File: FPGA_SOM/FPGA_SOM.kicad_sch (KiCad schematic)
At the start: 58 parts, among them J1 Conn_01x12, J2 Conn_02x05_Counter_Clockwise, J3 Conn_01x06, J5 Conn_01x02, J7 Conn_01x09, J8 Conn_01x10, U1 ICE40UP5K-SG48ITR, U101 W25X20CLSN, U2 AP2127N-3.3, U3 AP2127N-1.2, X101 ECS-2520MV-xxx-xx

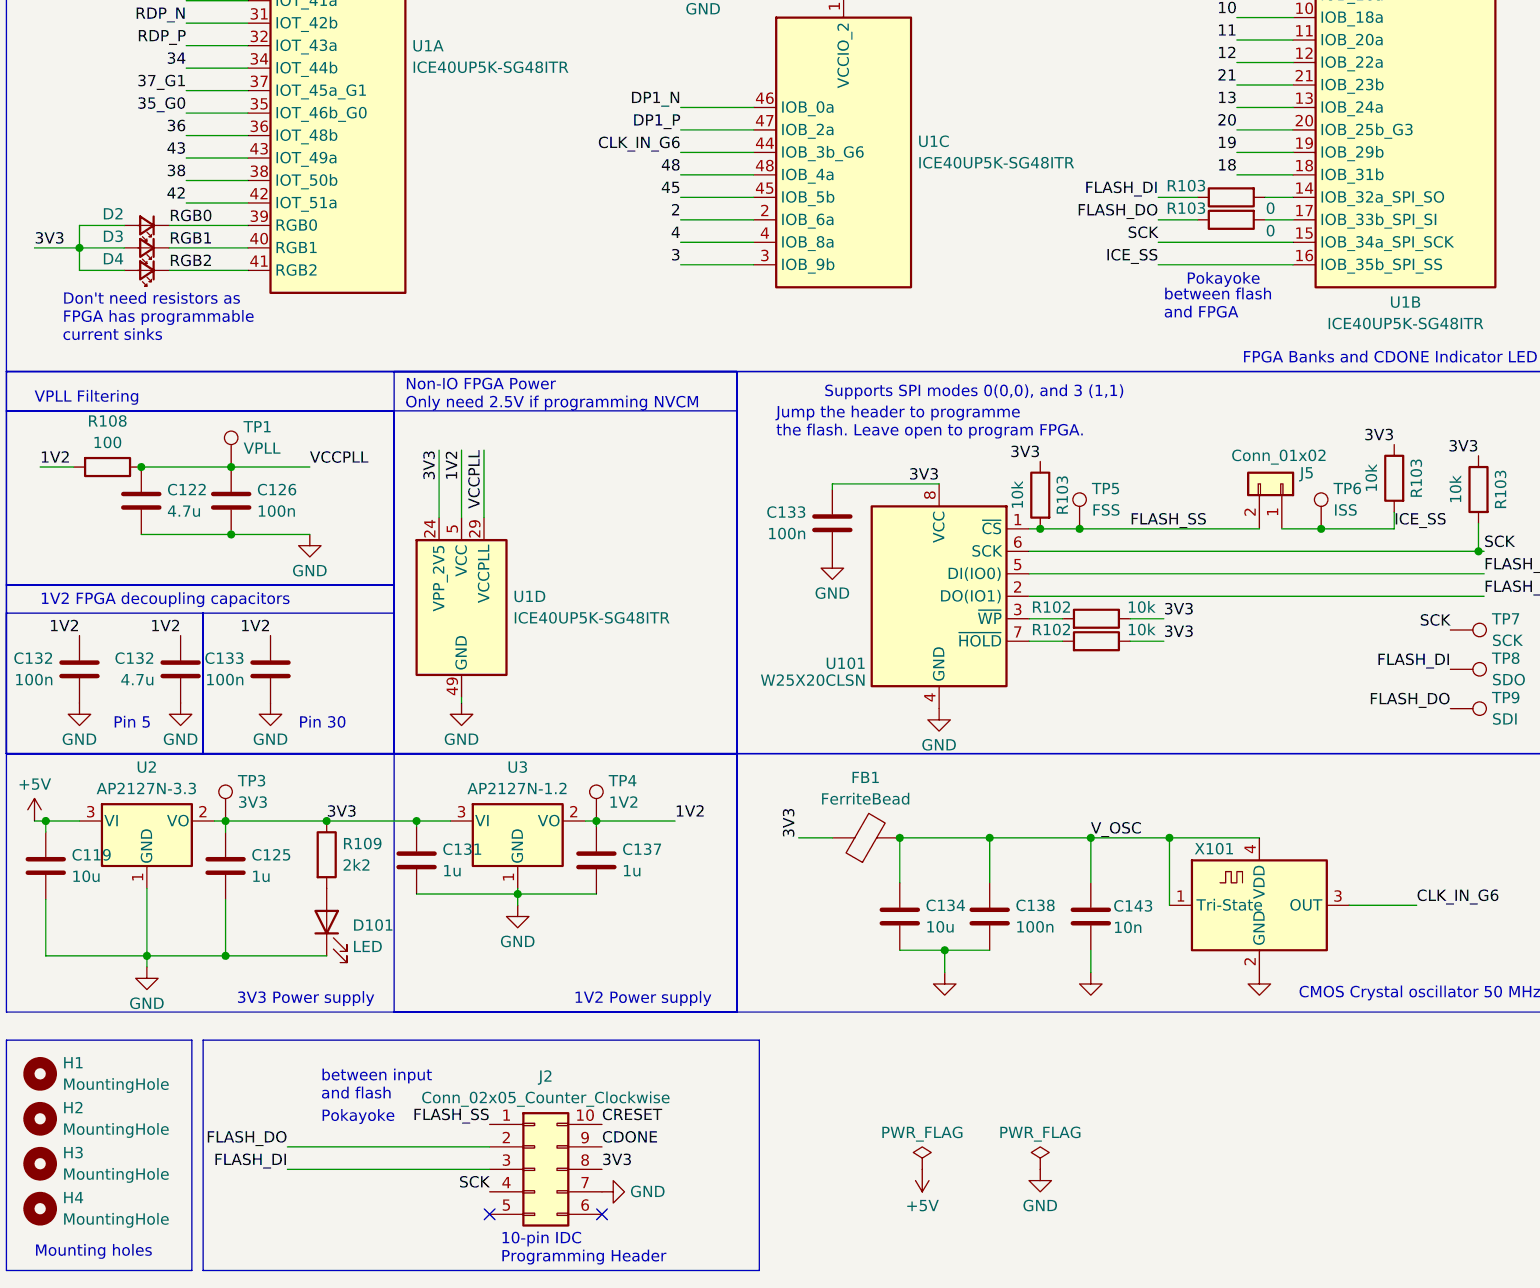
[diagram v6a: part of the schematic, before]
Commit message: Added button and clarified silkscreen for RGB leds.
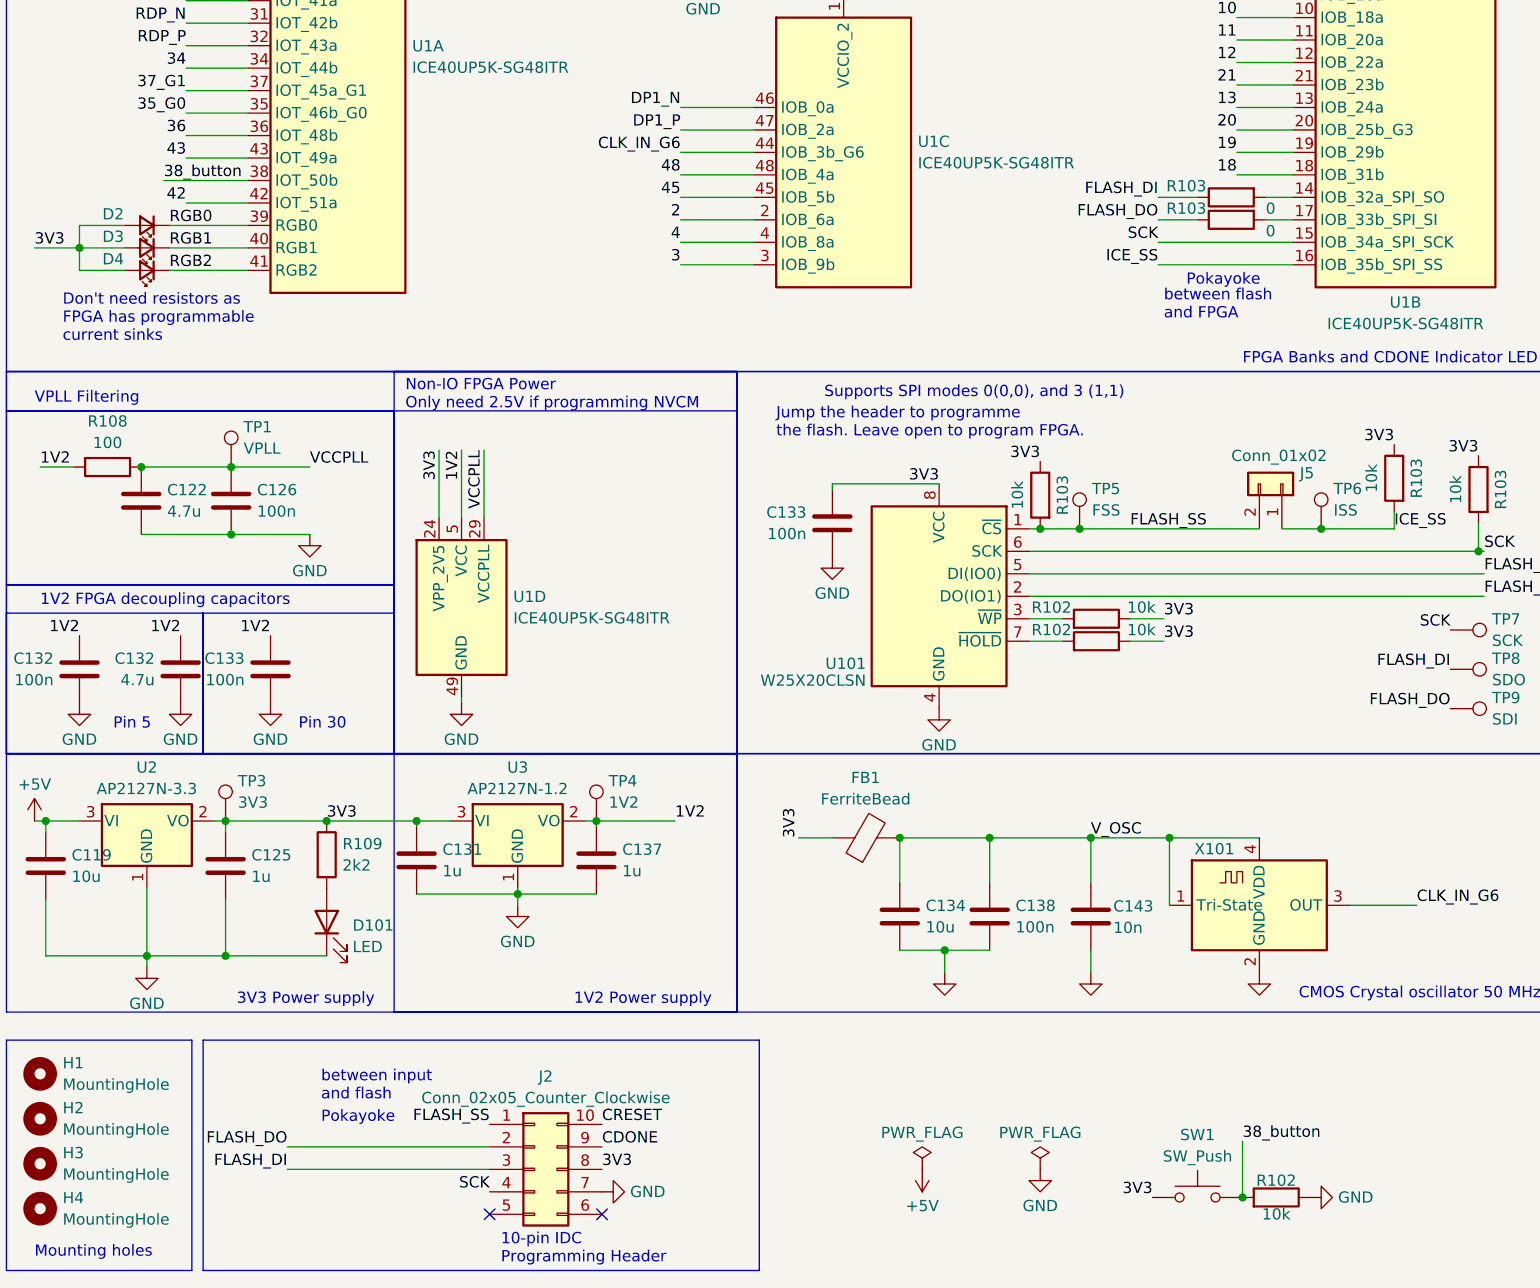
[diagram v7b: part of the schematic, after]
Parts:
- added R102: 10k, Resistor_SMD:R_0603_1608Metric, symbol Device:R
- added SW1: SW_Push, Button_Switch_THT:SW_PUSH_6mm, symbol Switch:SW_Push
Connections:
- net 38: no longer U1.38 (IOT_50b)
- net 3V3: now also SW1.1
- net GND: now also R102.1
- new net 38_button: R102.2, SW1.2, U1.38 (IOT_50b)
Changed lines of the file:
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@@
   (junction (at 155.575 19.685) (diameter 0) (color 0 0 0 0)
+  )
+  (junction (at 153.035 186.69) (diameter 0) (color 0 0 0 0)
   )
   (junction (at 49.53 144.145) (diameter 0) (color 0 0 0 0)
@@
     (stroke (width 0) (type default))
   )
+  (wire (pts (xy 153.035 180.34) (xy 153.035 186.69))
+    (stroke (width 0) (type default))
+  )
   (wire (pts (xy 143.51 78.74) (xy 158.75 78.74))
     (stroke (width 0) (type default))
@@
     (stroke (width 0) (type default))
   )
-  (wire (pts (xy 33.655 71.755) (xy 40.64 71.755))
+  (wire (pts (xy 31.115 71.755) (xy 40.64 71.755))
     (stroke (width 0) (type default))
   )
@@
     (effects (font (size 1.27 1.27)) (justify left bottom))
   )
-  (label "38" (at 33.655 71.755 180) (fields_autoplaced)
-    (effects (font (size 1.27 1.27)) (justify right bottom))
-  )
   (label "20" (at 152.4 66.04 180) (fields_autoplaced)
     (effects (font (size 1.27 1.27)) (justify right bottom))
@@
     (effects (font (size 1.27 1.27)) (justify left bottom))
   )
+  (label "3V3" (at 142.875 186.69 180) (fields_autoplaced)
+    (effects (font (size 1.27 1.27)) (justify right bottom))
+  )
   (label "FLASH_DI" (at 143.51 73.66 180) (fields_autoplaced)
     (effects (font (size 1.27 1.27)) (justify right bottom))
@@
     (effects (font (size 1.27 1.27)) (justify right bottom))
   )
+  (label "38_button" (at 31.115 71.755 0) (fields_autoplaced)
+    (effects (font (size 1.27 1.27)) (justify left bottom))
+  )
   (label "CDONE" (at 80.645 180.975 0) (fields_autoplaced)
     (effects (font (size 1.27 1.27)) (justify left bottom))
@@
   )
   (label "RGB0" (at 31.75 76.835 0) (fields_autoplaced)
+    (effects (font (size 1.27 1.27)) (justify left bottom))
+  )
+  (label "38_button" (at 153.035 180.34 0) (fields_autoplaced)
     (effects (font (size 1.27 1.27)) (justify left bottom))
   )
@@
     )
   )
+  (symbol (lib_id "Switch:SW_Push") (at 147.955 186.69 0) (unit 1)
+    (in_bom yes) (on_board yes) (dnp no) (fields_autoplaced)
+    (property "Reference" "SW1" (at 147.955 179.6247 0)
+      (effects (font (size 1.27 1.27)))
+    )
+    (property "Value" "SW_Push" (at 147.955 182.0489 0)
+      (effects (font (size 1.27 1.27)))
+    )
+    (property "Footprint" "Button_Switch_THT:SW_PUSH_6mm" (at 147.955 181.61 0)
+      (effects (font (size 1.27 1.27)) hide)
+    )
+    (property "Datasheet" "~" (at 147.955 181.61 0)
+      (effects (font (size 1.27 1.27)) hide)
+    )
+    (pin "1")
+    (pin "2")
+    (instances
+      (project "FPGA_SOM"
+        (path "/c9513ae4-ec90-4b73-ae24-d135d02c4e68"
+          (reference "SW1") (unit 1)
+        )
+      )
+    )
+  )
   (symbol (lib_id "Device:C") (at 28.575 107.95 0) (unit 1)
     (in_bom yes) (on_board yes) (dnp no)
@@
         (path "/c9513ae4-ec90-4b73-ae24-d135d02c4e68"
           (reference "#PWR06") (unit 1)
+        )
+      )
+    )
+  )
+  (symbol (lib_id "power:GND") (at 160.655 186.69 90) (unit 1)
+    (in_bom yes) (on_board yes) (dnp no) (fields_autoplaced)
+    (property "Reference" "#PWR022" (at 167.005 186.69 0)
+      (effects (font (size 1.27 1.27)) hide)
+    )
+    (property "Value" "GND" (at 163.83 186.69 90)
+      (effects (font (size 1.27 1.27)) (justify right))
+    )
+    (property "Footprint" "" (at 160.655 186.69 0)
+      (effects (font (size 1.27 1.27)) hide)
+    )
+    (property "Datasheet" "" (at 160.655 186.69 0)
+      (effects (font (size 1.27 1.27)) hide)
+    )
+    (pin "1")
+    (instances
+      (project "FPGA_SOM"
+        (path "/c9513ae4-ec90-4b73-ae24-d135d02c4e68"
+          (reference "#PWR022") (unit 1)
         )
       )
@@
         )
       )
+    )
+  )
+  (symbol (lib_id "Device:R") (at 156.845 186.69 270) (mirror x) (unit 1)
+    (in_bom yes) (on_board yes) (dnp no)
+    (property "Reference" "R102" (at 156.845 184.785 90)
+      (effects (font (size 1.27 1.27)))
+    )
+    (property "Value" "10k" (at 156.845 188.595 90)
+      (effects (font (size 1.27 1.27)))
+    )
+    (property "Footprint" "Resistor_SMD:R_0603_1608Metric" (at 156.845 188.468 90)
+      (effects (font (size 1.27 1.27)) hide)
+    )
+    (property "Datasheet" "https://www.digikey.co.nz/en/products/detail/yageo/AC0603FR-1310KL/13694194" (at 156.845 186.69 0)
+      (effects (font (size 1.27 1.27)) hide)
+    )
+    (property "Price" "" (at 156.845 186.69 0)
+      (effects (font (size 1.27 1.27)) hide)
+    )
+    (pin "1")
+    (pin "2")
+    (instances
+      (project "ICE40Breakout"
+        (path "/7a8e4b43-2524-4863-bf7c-adf3dbbc9623"
+          (reference "R102") (unit 1)
+        )
+      )
+      (project "FPGA_SOM"
+        (path "/c9513ae4-ec90-4b73-ae24-d135d02c4e68"
+          (reference "R12") (unit 1)
+        )
+      )

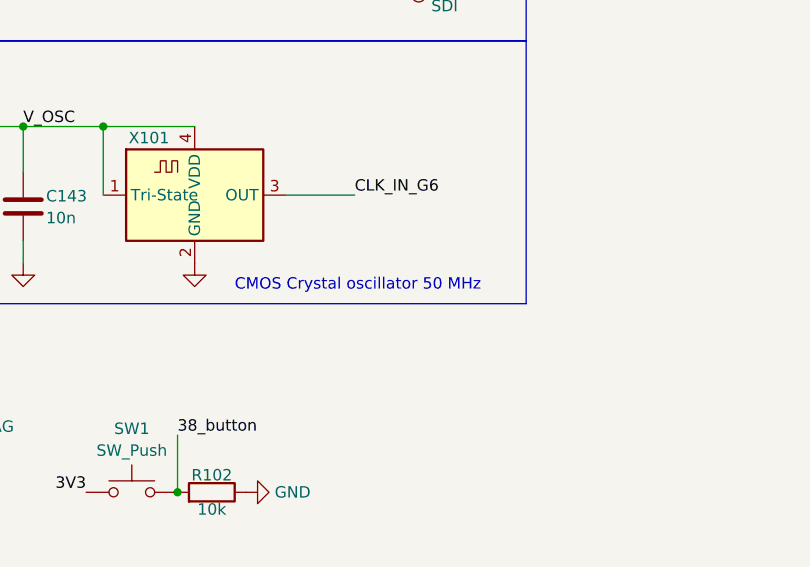
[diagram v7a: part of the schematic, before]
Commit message: Added silkscreen, stitching vias, and quality of life improvements.
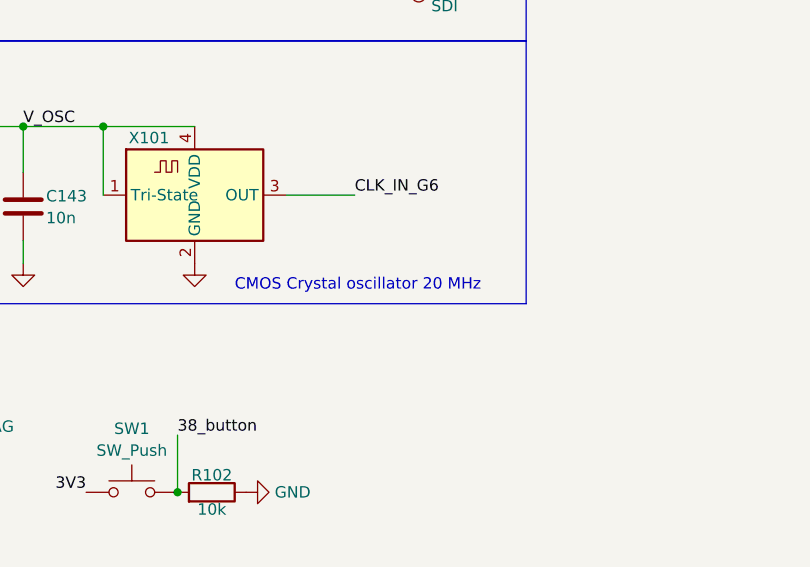
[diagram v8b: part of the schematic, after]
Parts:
- H1, H2, H3, H4: footprint MountingHole:MountingHole_3.2mm_M3 -> MountingHole:MountingHole_3.2mm_M3_DIN965_Pad
- TP1, TP3, TP4, TP5, TP6, TP7, TP8, TP9: footprint TestPoint:TestPoint_Pad_2.0x2.0mm -> TestPoint:TestPoint_THTPad_D2.0mm_Drill1.0mm
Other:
- note added: "CMOS Crystal oscillator 20 MHz"
- note removed: "CMOS Crystal oscillator 50 MHz"
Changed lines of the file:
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@@
     (effects (font (size 1.27 1.27)) (justify left bottom))
   )
-  (text "CMOS Crystal oscillator 50 MHz" (at 159.385 164.465 0)
+  (text "CMOS Crystal oscillator 20 MHz" (at 159.385 164.465 0)
     (effects (font (size 1.27 1.27)) (justify left bottom))
   )
@@
       (effects (font (size 1.27 1.27)) (justify left))
     )
-    (property "Footprint" "TestPoint:TestPoint_Pad_2.0x2.0mm" (at 176.53 136.525 0)
+    (property "Footprint" "TestPoint:TestPoint_THTPad_D2.0mm_Drill1.0mm" (at 176.53 136.525 0)
       (effects (font (size 1.27 1.27)) hide)
     )
@@
       (effects (font (size 1.27 1.27)) (justify left))
     )
-    (property "Footprint" "TestPoint:TestPoint_Pad_2.0x2.0mm" (at 43.815 104.14 0)
+    (property "Footprint" "TestPoint:TestPoint_THTPad_D2.0mm_Drill1.0mm" (at 43.815 104.14 0)
       (effects (font (size 1.27 1.27)) hide)
     )
@@
       (effects (font (size 1.27 1.27)) (justify left))
     )
-    (property "Footprint" "MountingHole:MountingHole_3.2mm_M3" (at 17.145 182.88 0)
+    (property "Footprint" "MountingHole:MountingHole_3.2mm_M3_DIN965_Pad" (at 17.145 182.88 0)
       (effects (font (size 1.27 1.27)) hide)
     )
@@
       (effects (font (size 1.27 1.27)) (justify left))
     )
-    (property "Footprint" "MountingHole:MountingHole_3.2mm_M3" (at 17.145 177.8 0)
+    (property "Footprint" "MountingHole:MountingHole_3.2mm_M3_DIN965_Pad" (at 17.145 177.8 0)
       (effects (font (size 1.27 1.27)) hide)
     )
@@
       (effects (font (size 1.27 1.27)) (justify left))
     )
-    (property "Footprint" "TestPoint:TestPoint_Pad_2.0x2.0mm" (at 176.53 132.08 0)
+    (property "Footprint" "TestPoint:TestPoint_THTPad_D2.0mm_Drill1.0mm" (at 176.53 132.08 0)
       (effects (font (size 1.27 1.27)) hide)
     )
@@
       (effects (font (size 1.27 1.27)) (justify left))
     )
-    (property "Footprint" "TestPoint:TestPoint_Pad_2.0x2.0mm" (at 176.53 127.635 0)
+    (property "Footprint" "TestPoint:TestPoint_THTPad_D2.0mm_Drill1.0mm" (at 176.53 127.635 0)
       (effects (font (size 1.27 1.27)) hide)
     )
@@
       (effects (font (size 1.27 1.27)) (justify left))
     )
-    (property "Footprint" "TestPoint:TestPoint_Pad_2.0x2.0mm" (at 139.7 111.125 0)
+    (property "Footprint" "TestPoint:TestPoint_THTPad_D2.0mm_Drill1.0mm" (at 139.7 111.125 0)
       (effects (font (size 1.27 1.27)) hide)
     )
@@
       (effects (font (size 1.27 1.27)) (justify left))
     )
-    (property "Footprint" "MountingHole:MountingHole_3.2mm_M3" (at 17.145 187.96 0)
+    (property "Footprint" "MountingHole:MountingHole_3.2mm_M3_DIN965_Pad" (at 17.145 187.96 0)
       (effects (font (size 1.27 1.27)) hide)
     )
@@
       (effects (font (size 1.27 1.27)) (justify left))
     )
-    (property "Footprint" "TestPoint:TestPoint_Pad_2.0x2.0mm" (at 43.18 144.145 0)
+    (property "Footprint" "TestPoint:TestPoint_THTPad_D2.0mm_Drill1.0mm" (at 43.18 144.145 0)
       (effects (font (size 1.27 1.27)) hide)
     )
@@
       (effects (font (size 1.27 1.27)) (justify left))
     )
-    (property "Footprint" "MountingHole:MountingHole_3.2mm_M3" (at 17.145 172.72 0)
+    (property "Footprint" "MountingHole:MountingHole_3.2mm_M3_DIN965_Pad" (at 17.145 172.72 0)
       (effects (font (size 1.27 1.27)) hide)
     )
@@
       (effects (font (size 1.27 1.27)) (justify left))
     )
-    (property "Footprint" "TestPoint:TestPoint_Pad_2.0x2.0mm" (at 167.005 111.125 0)
+    (property "Footprint" "TestPoint:TestPoint_THTPad_D2.0mm_Drill1.0mm" (at 167.005 111.125 0)
       (effects (font (size 1.27 1.27)) hide)
     )
@@
       (effects (font (size 1.27 1.27)) (justify left))
     )
-    (property "Footprint" "TestPoint:TestPoint_Pad_2.0x2.0mm" (at 85.09 144.145 0)
-      (effects (font (size 1.27 1.27)) hide)
-    )
+    (property "Footprint" "TestPoint:TestPoint_THTPad_D2.0mm_Drill1.0mm" (at 85.09 144.145 0)
+      (effects (font (size 1.27 1.27)) hide)
+    )
